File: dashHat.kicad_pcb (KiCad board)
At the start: 4 copper layers, 65 x 56 mm, 146 parts, among them J1 Input, J2 LCD, J3 GPIO, J4 LEDs, J5 Ride Through, J6 SMA, J7 Conn_01x08, Q1 BSS138, Q2 BSS138, Q3 2N7002, Q4 BSS84, Q5 BSS84, Q6 BSS84, Q7 , Q8 , Q9 BSS84, U1 CAT24C256, U12 MAX22193, U13 IX4427, U2 MAX17614, U3 TVS3300DRV, U4 LM61480, U5 74LVC1G80, U6 ZOE-M8Q, U7 TCAN330, U8 MCP2515-xST, U9 MAX3227, Y1 32.768k, Y2 8MHz

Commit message: fixes from testing, updated for pi5
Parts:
- removed TP1, TP2: TestPoint, TestPoint:TestPoint_Pad_1.0x1.0mm
- R1, R3: value 10k -> 1.8k
- R35: value 18k -> 5.1k
- R36, R37, R38, R39: value 1.5k -> 430
- moved J7 0.48 mm to (162.6, 73.6)
- moved J4 0.40 mm to (160.1, 52.9)
- moved F1 0.23 mm to (149.9, 69.0)
- turned U8 to 90 degrees
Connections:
- J7 pad 7: Net-(D18-A) -> Net-(D19-A)
- J7 pad 8: Net-(D19-A) -> Net-(D18-A)
- U12 pad 10: /GPIO5 -> /GPIO6
- U12 pad 9: /GPIO6 -> /GPIO19/PCM.FS
- U6 pad J4: Net-(U6-RXD/SPI_MOSI) -> /GPIO4/GPCLK0
- U6 pad J5: Net-(U6-TXD/SPI_MISO) -> /GPIO5
- U8 pad 1: Net-(U7-TXD) -> unconnected-(U8-CLKOUT/SOF-Pad1)
- U8 pad 10: GND -> unconnected-(U8-~{RX0BF}-Pad10)
- U8 pad 11: unconnected-(U8-~{RX1BF}-Pad11) -> /GPIO25
- U8 pad 12: unconnected-(U8-~{RX0BF}-Pad12) -> /GPIO11/SPI0.SCLK
- U8 pad 13: /GPIO25 -> unconnected-(U8-NC-Pad13)
- U8 pad 14: /GPIO11/SPI0.SCLK -> /GPIO10/SPI0.MOSI
- U8 pad 15: unconnected-(U8-NC-Pad15) -> /GPIO9/SPI0.MISO
- U8 pad 16: /GPIO10/SPI0.MOSI -> /GPIO8/SPI0.CE0
- U8 pad 17: /GPIO9/SPI0.MISO -> Net-(U8-~{RESET})
- U8 pad 18: /GPIO8/SPI0.CE0 -> +3V3
- U8 pad 19: Net-(U8-~{RESET}) -> Net-(U7-TXD)
- U8 pad 2: Net-(Q4-G) -> unconnected-(U8-~{TX0RTS}-Pad2)
- U8 pad 20: +3V3 -> Net-(Q4-G)
- U8 pad 21: (no net) -> GND
- U8 pad 6: unconnected-(U8-NC-Pad6) -> Net-(U8-OSC2)
- U8 pad 7: unconnected-(U8-~{TX2RTS}-Pad7) -> Net-(U8-OSC1)
- U8 pad 8: Net-(U8-OSC2) -> GND
- U8 pad 9: Net-(U8-OSC1) -> unconnected-(U8-~{RX1BF}-Pad9)
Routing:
- net /GPIO19/PCM.FS: track 0.00 -> 30.5 mm
- net /GPIO4/GPCLK0: track 0.00 -> 25.8 mm, vias 0 -> 1
- net /GPIO5: track 37.3 -> 60.1 mm, vias 0 -> 2
- net Net-(U8-OSC1): track 7.50 -> 12.9 mm
- net Net-(U8-OSC2): track 5.23 -> 9.82 mm
- net GND: track 96.1 -> 92.0 mm, vias 131 -> 124
- net /GPIO25: track 15.4 -> 12.0 mm
- net /GPIO11/SPI0.SCLK: track 6.92 -> 3.78 mm
- net Net-(U8-~{RESET}): track 8.43 -> 5.57 mm
- net +5V: track 90.7 -> 88.4 mm, vias 19 -> 29
- net Net-(U6-RXD/SPI_MOSI): track 2.32 -> 0.00 mm
- net Net-(U6-TXD/SPI_MISO): track 2.22 -> 0.00 mm, vias 1 -> 0
- net Net-(U7-TXD): track 26.3 -> 24.3 mm
- net +3V3: track 178.6 -> 180.1 mm
- net Net-(Q4-G): track 25.5 -> 24.1 mm
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
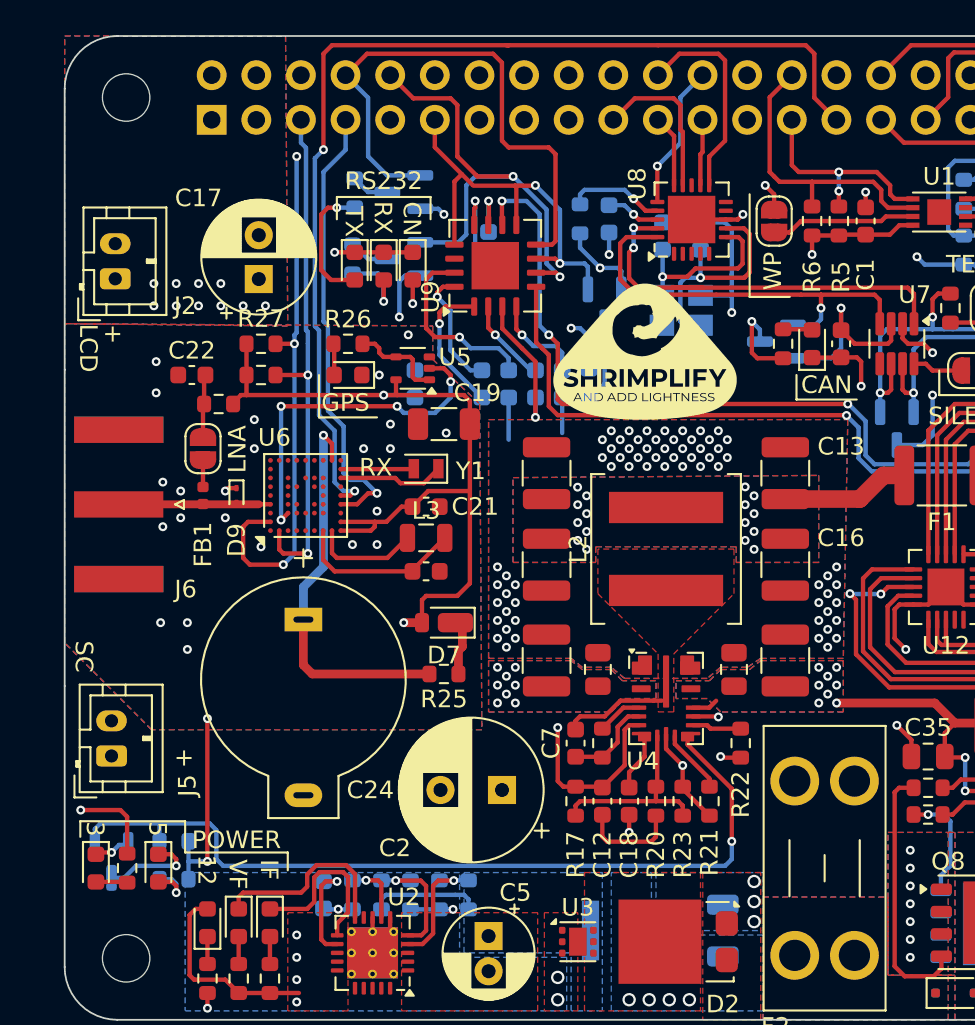
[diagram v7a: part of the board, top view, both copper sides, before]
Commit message: added a switch to the lcd, and feedback from the 12v input to the pi
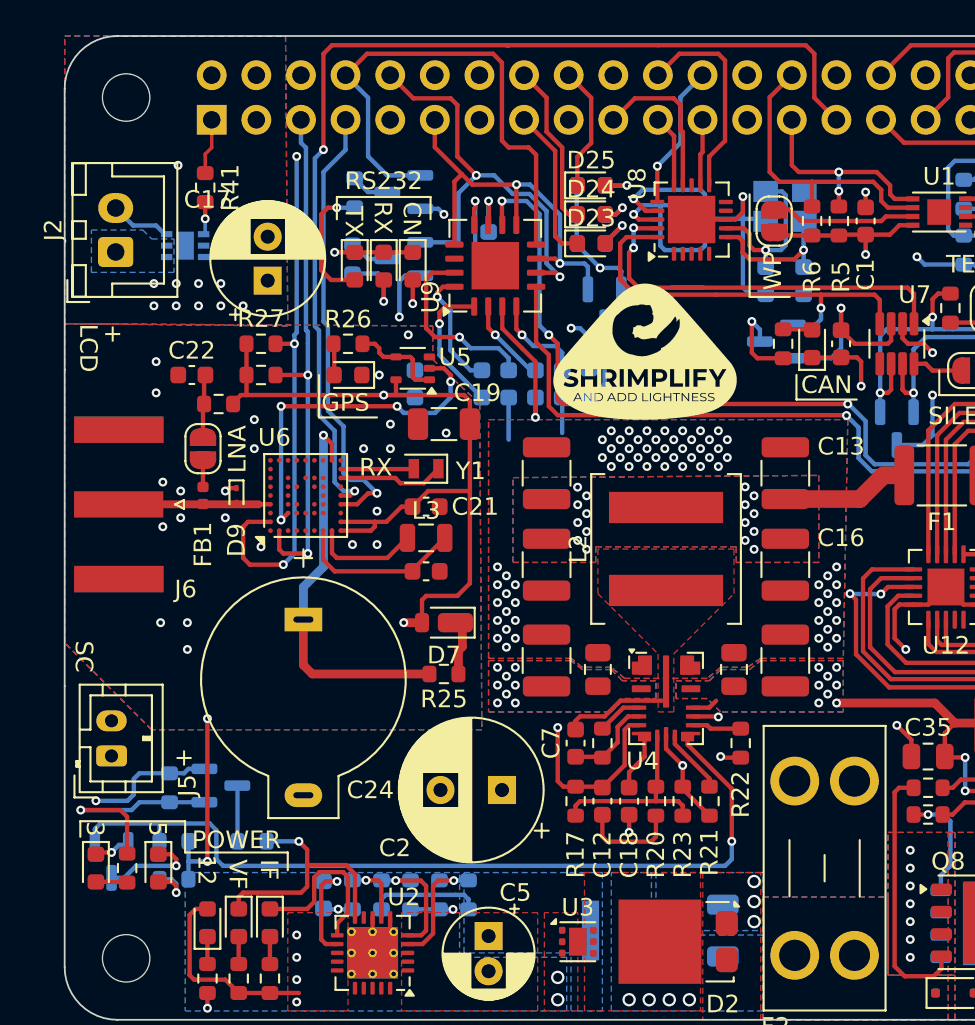
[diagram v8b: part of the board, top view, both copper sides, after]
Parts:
- added D23: Green, LED_SMD:LED_0603_1608Metric, F.Cu at (130.0, 55.8)
- added D24: Green, LED_SMD:LED_0603_1608Metric, F.Cu at (130.0, 54.2)
- added D25: Green, LED_SMD:LED_0603_1608Metric, F.Cu at (130.0, 52.5)
- added Q10: ADP197, Package_DFN_QFN:DFN-6-1EP_2x2mm_P0.65mm_EP1x1.6mm, B.Cu at (106.9, 55.9)
- added Q12: BSS138, Package_TO_SOT_SMD:SOT-23, B.Cu at (108.9, 86.7)
- added R41: 10k, Resistor_SMD:R_0603_1608Metric, F.Cu at (108.0, 52.6)
- added R43: 220, Resistor_SMD:R_0603_1608Metric, B.Cu at (130.0, 55.8)
- added R46: 220, Resistor_SMD:R_0603_1608Metric, B.Cu at (130.0, 54.2)
- added R47: 220, Resistor_SMD:R_0603_1608Metric, B.Cu at (130.0, 52.5)
- added R49: 10k, Resistor_SMD:R_0603_1608Metric, B.Cu at (110.7, 89.8)
- added R50: 10k, Resistor_SMD:R_0603_1608Metric, B.Cu at (106.0, 86.8)
- J2: footprint Connector_JST:JST_PH_B2B-PH-K_1x02_P2.00mm_Vertical -> Connector_JST:JST_XH_B2B-XH-A_1x02_P2.50mm_Vertical
- moved C26 8.42 mm to (142.1, 57.9), turned to -90 degrees
- moved Y2 8.36 mm to (141.0, 53.7), turned to 180 degrees
- moved R30 7.11 mm to (136.4, 54.4)
- moved C27 4.50 mm to (139.9, 57.9), turned to -90 degrees
- moved C28 3.94 mm to (134.9, 54.4)
- moved J2 1.53 mm to (102.9, 56.3)
- moved C17 0.52 mm to (111.6, 57.9)
- turned JP1 to -90 degrees
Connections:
- J2 pad 1: +5V -> Net-(J2-Pin_1)
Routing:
- net /GPIO27: track 0.00 -> 76.3 mm, vias 0 -> 2
- net /GPIO18/PCM.CLK: track 0.00 -> 26.4 mm, vias 0 -> 1
- net +3V3: track 180.1 -> 200.9 mm, vias 15 -> 14
- net /GPIO23: track 0.00 -> 9.46 mm
- net /GPIO22: track 0.00 -> 8.80 mm
- net /GPIO24: track 0.00 -> 7.13 mm
- net GND: track 92.0 -> 98.7 mm, vias 124 -> 122
- net Net-(D5-K): track 11.1 -> 14.9 mm, vias 0 -> 1
- net Net-(U8-OSC1): track 12.9 -> 9.47 mm
- net Net-(Q12-D): track 0.00 -> 3.29 mm
- net Net-(D23-A): track 0.00 -> 2.83 mm, vias 0 -> 1
- net Net-(D25-A): track 0.00 -> 2.45 mm, vias 0 -> 1
- net Net-(D24-A): track 0.00 -> 2.26 mm, vias 0 -> 1
- net /GPIO15/RXD0: track 27.9 -> 25.7 mm
- net /GPIO14/TXD0: track 32.1 -> 30.0 mm
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- added copper zone on B.Cu, net Net-(J2-Pin_1)
